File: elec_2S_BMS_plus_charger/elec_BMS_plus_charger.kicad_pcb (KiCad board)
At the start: 2 copper layers, 46 x 24 mm, 52 parts, among them J1 JST -EH 2, J13 Dynamixel-3, J14 Dynamixel-3, J2 JST SH, J3 JST -EH 2, J4 JST -EH 2, J5 pico2, J6 pico2, J7 JST SH, Q1 BSZ034N04LS, Q2 BSZ034N04LS, U1 HY2120, U2 BQ25887RGE

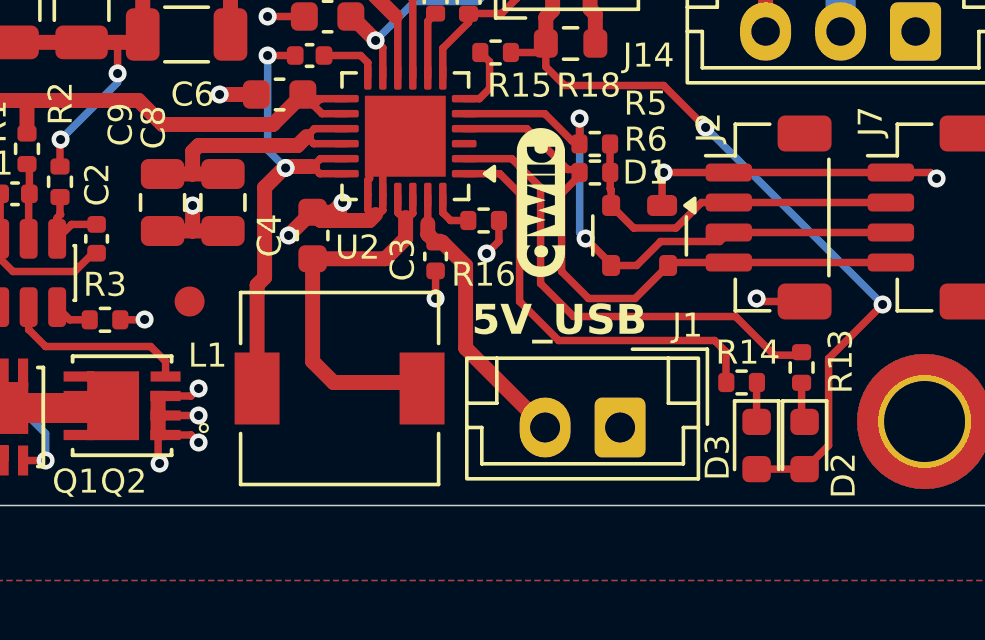
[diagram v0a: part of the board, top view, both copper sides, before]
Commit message: [update] Now running test on rasp zero 2W + HAT
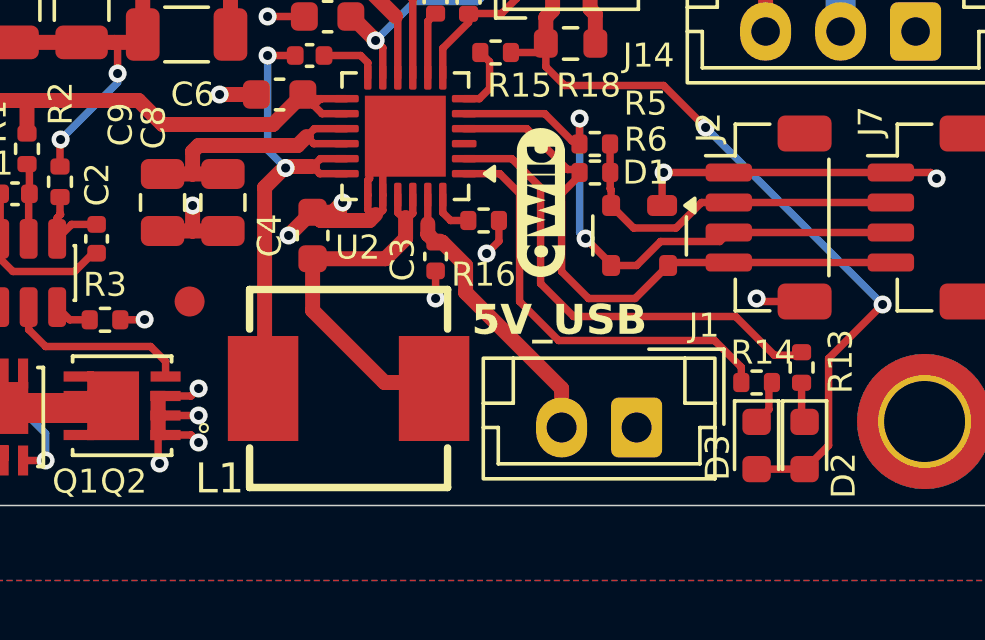
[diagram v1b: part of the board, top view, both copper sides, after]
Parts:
- L1: footprint Inductor_SMD:L_6.3x6.3_H3 -> LCSC_parts_lib:IND-SMD_L7.2-W6.6_GPSR0730
- moved J1 0.55 mm to (158.3, 79.5)
- moved R14 0.50 mm to (162.3, 78.0)
- moved L1 0.30 mm to (148.7, 78.2)
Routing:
- net Net-(C4-Pad1): track 13.3 -> 12.4 mm
